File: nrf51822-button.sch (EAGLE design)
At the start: 26 parts, among them U1 nRF51822, X1 16MHz, X2 32.768kHz

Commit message: Clean up! This might acutally work (!). Removd 32KHz crystal, added 20 uF of bulk cap for spikes (might need more?). Biggest problem: antenna ok? Do we need the DC-DC converter to reduce the current load on the CR1632 battery? Stay tuned!
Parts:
- removed C11: 12pF, rcl_custom:C-EU0402-C-NOSILK
- removed X2: 32.768kHz, AMLib:CRYSTAL'2012'
- added C10: 10u, rcl_custom:C-EU0805-B-NOSILK
- added JP1: (no value), SparkFun-v5:M041.27MM
- C1, C14, C3: value 100nF -> 100n
- C12, C13: value 12pF -> 12p
- C2: value 1nF -> 1n
- C4: value 47nF -> 47n
- C5: value 12pF -> 10u; device rcl_custom:C-EU0402-C-NOSILK -> rcl_custom:C-EU0805-B-NOSILK
- C6: value 2.2pF -> 2.2p
- C7: value 1.0pF -> 1.0p
- C8: value 1.5pF -> 1.5p
- C9: value 2.2nF -> 2.2n
- L1: value 4.7nH -> 4.7n
- L2: value 10nH -> 10n
- L3: value 3.3nH -> 3.3n
- R1, R2: value 12k -> 10k
- U1: value nRF51822 -> NRF51822-QFAB-R7
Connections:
- net ROUTE-ANT renamed ANTENNA
- removed net N$14: C5.2, U1.P0.26/AIN0/XL2_32768E, X2.2
- removed net N$16: C11.2, U1.P0.27/AIN1/XL1_32768I, X2.1
- net GND: now also C10.2, C5.2, JP1.4; no longer C11.1, C5.1
- net N$1: now also U1.P0.00/AREF0; no longer U1.P0.30
- net N$2: now also U1.P0.01/AIN2; no longer U1.P0.00/AREF0
- net N$3: now also U1.P0.02/AIN3; no longer U1.P0.01/AIN2
- net SWDCLK: now also JP1.3
- net SWDIO: now also JP1.2
- net VDD: now also C10.1, C5.1, JP1.1
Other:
- note added: "128K part in QFN48 package"
- note added: "CR1632 battery holder (16 mm x 3.2mm)"
- note added: "FIXME"
- note added: "NRF51822-QFAB-R7"
- note added: "SWD Programmer"
- moved on the sheet: C5, R1, R2

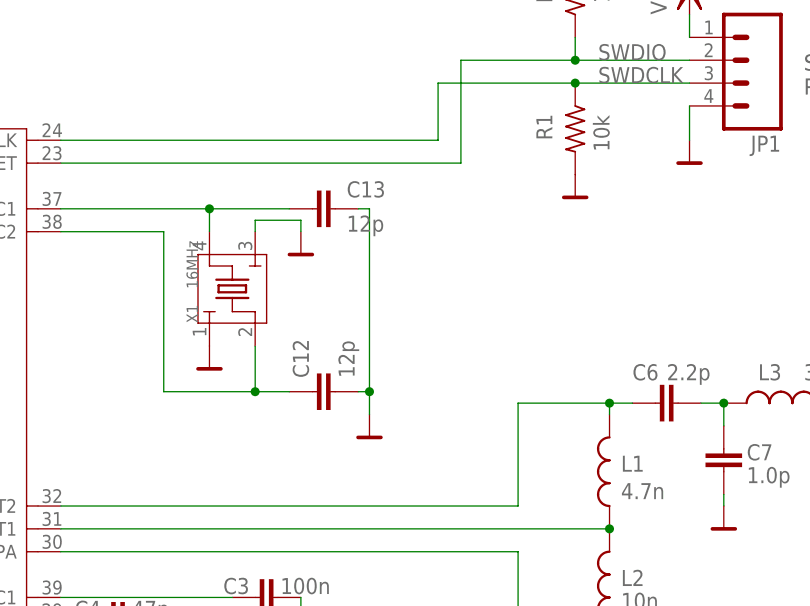
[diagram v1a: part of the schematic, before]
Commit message: Final board cleanup, including checking values and packages. Routed this one as a prototype on the A406. Also added BOM.
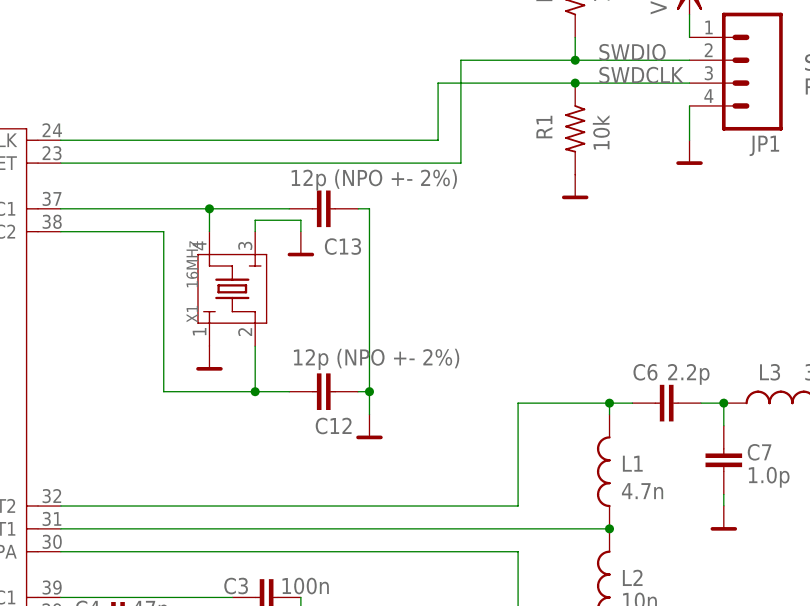
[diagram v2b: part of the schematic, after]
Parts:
- C12, C13: value 12p -> 12p (NPO +- 2%)
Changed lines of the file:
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@@
 <setting verticaltext="up"/>
 </settings>
-<grid distance="0.05" unitdist="inch" unit="inch" style="lines" multiple="2" display="no" altdistance="0.01" altunitdist="inch" altunit="inch"/>
+<grid distance="0.05" unitdist="inch" unit="inch" style="lines" multiple="2" display="yes" altdistance="0.01" altunitdist="inch" altunit="inch"/>
 <layers>
 <layer number="1" name="Top" color="4" fill="1" visible="no" active="no"/>
@@
 <parts>
 <part name="U1" library="AMLib" deviceset="NRF51822" device="" value="NRF51822-QFAB-R7"/>
-<part name="C12" library="rcl_custom" deviceset="C-EU" device="0402-C-NOSILK" value="12p"/>
-<part name="C13" library="rcl_custom" deviceset="C-EU" device="0402-C-NOSILK" value="12p"/>
+<part name="C12" library="rcl_custom" deviceset="C-EU" device="0402-C-NOSILK" value="12p (NPO +- 2%)"/>
+<part name="C13" library="rcl_custom" deviceset="C-EU" device="0402-C-NOSILK" value="12p (NPO +- 2%)"/>
 <part name="C1" library="rcl_custom" deviceset="C-EU" device="0402-C-NOSILK" value="100n"/>
 <part name="C2" library="rcl_custom" deviceset="C-EU" device="0402-C-NOSILK" value="1n"/>
@@
 </instance>
 <instance part="C12" gate="CE" x="156.21" y="109.22" smashed="yes" rot="R90">
-<attribute name="NAME" x="155.829" y="110.744" size="1.778" layer="95" rot="R90"/>
-<attribute name="VALUE" x="160.909" y="110.744" size="1.778" layer="96" rot="R90"/>
+<attribute name="NAME" x="156.464" y="104.521" size="1.778" layer="95"/>
+<attribute name="VALUE" x="153.924" y="112.141" size="1.778" layer="96"/>
 </instance>
 <instance part="C13" gate="CE" x="156.21" y="129.54" smashed="yes" rot="R90">
-<attribute name="NAME" x="160.02" y="130.81" size="1.778" layer="95"/>
-<attribute name="VALUE" x="160.02" y="127" size="1.778" layer="96"/>
+<attribute name="NAME" x="157.48" y="124.46" size="1.778" layer="95"/>
+<attribute name="VALUE" x="153.67" y="132.08" size="1.778" layer="96"/>
 </instance>
 <instance part="C1" gate="CE" x="142.24" y="53.34" smashed="yes">
